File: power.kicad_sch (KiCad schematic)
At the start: 62 parts, among them Q2 NTR5105PT1G, Q5 NX138BKWX, Q9 BC846BS

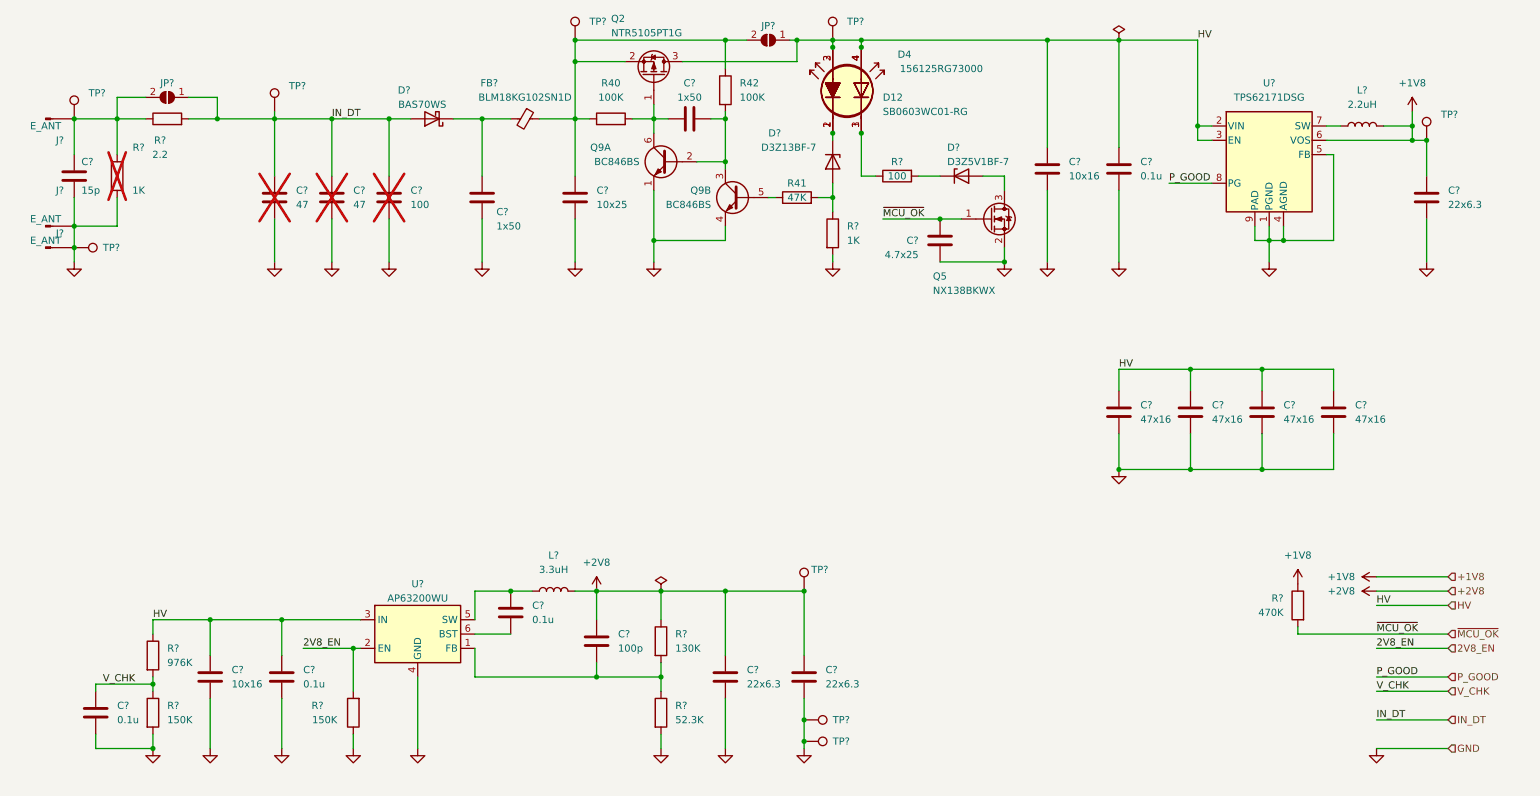
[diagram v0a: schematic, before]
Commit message: Fix capacitor values
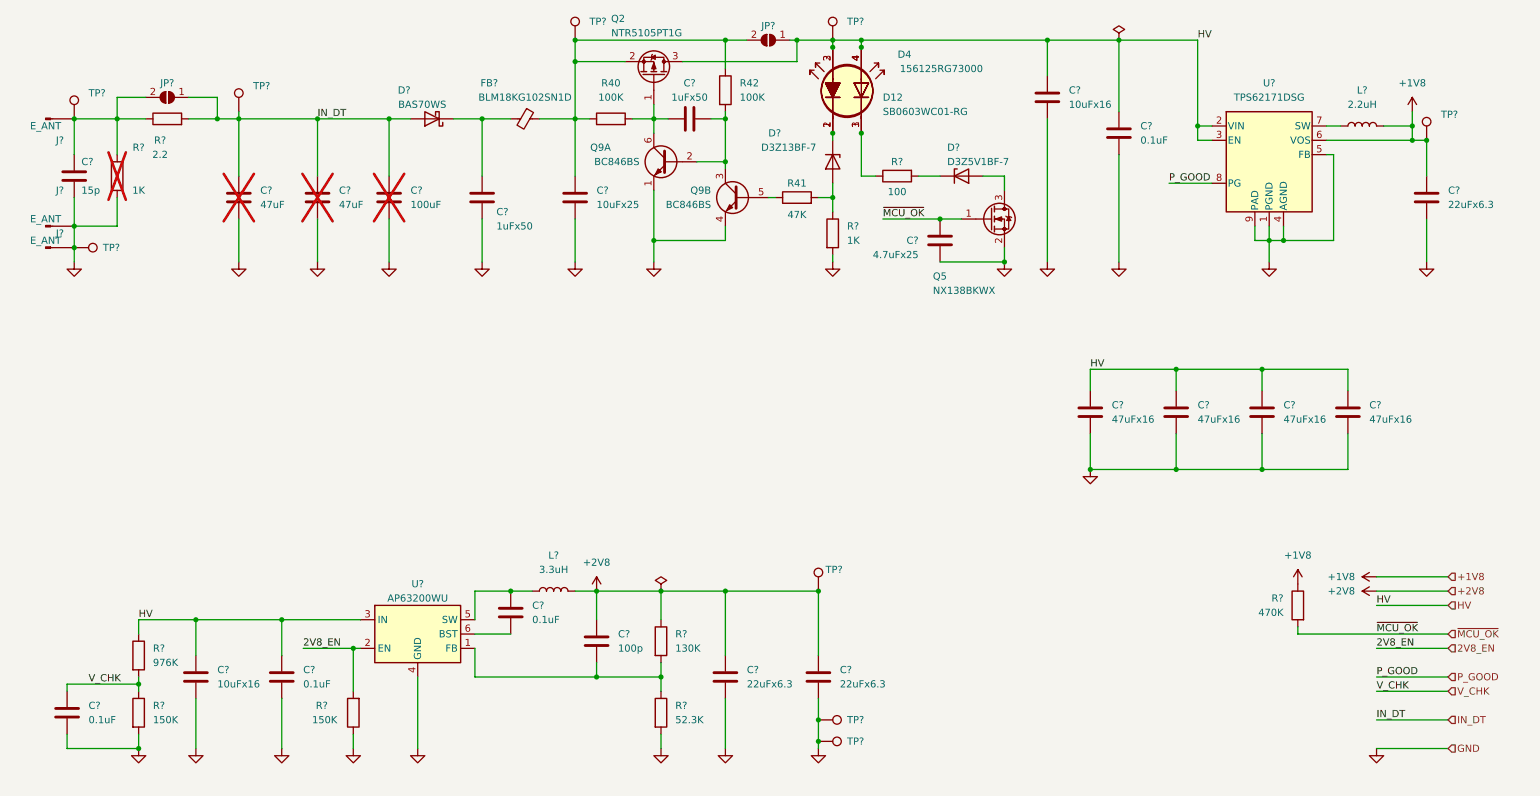
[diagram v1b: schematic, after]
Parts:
- C? (x2): value 1x50 -> 1uFx50
- C? (x4): value 47x16 -> 47uFx16
- C? (x4): value 0.1u -> 0.1uF
- C? (x3): value 22x6.3 -> 22uFx6.3
- C?: value 100 -> 100uF
- C? (x2): value 10x16 -> 10uFx16
- C?: value 10x25 -> 10uFx25
- C? (x2): value 47 -> 47uF
- C?: value 4.7x25 -> 4.7uFx25
- D?: value D3Z13BF-7 -> D3Z13BF-7
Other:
- moved on the sheet: C?, R?, TP?

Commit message: Fill up mouser part numbers
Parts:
- C? (x2): MouserPN (none) -> 81-GRM155R61H105ME5J
- C? (x4): MouserPN (none) -> 581-1210YG474ZAT2A
- C? (x4): MouserPN (none) -> 581-KGM05AR71C104KN
- C?: MouserPN (none) -> 187-CL05C101JC51PNC
- C? (x3): MouserPN (none) -> 581-KAM15CT70J226KT
- C?: MouserPN (none) -> 581-06035A150KAT2A
- C? (x3): now left out of the parts list
- C? (x2): MouserPN (none) -> 81-GRM188C81C106MA3D
- C?: MouserPN (none) -> 81-GRM188R61E106MA3D
- C?: MouserPN (none) -> 581-02013A100J
- D12: MouserPN (none) -> 593-SB0603WC01-RG
- D4: MouserPN (none) -> 710-156125RG73000
- D?: MouserPN (none) -> 241-BAS70WS_R1_00001
- D?: MouserPN (none) -> 621-D3Z5V1BF-7
- D?: MouserPN (none) -> 621-D3Z13BF-7
- FB?: MouserPN (none) -> 81-BLM18KG102SN1D
- L?: MouserPN (none) -> 710-74438335033
- Q2: MouserPN (none) -> 863-NTR5105PT1G
- Q5: MouserPN (none) -> 771-NX138BKWX
- Q9: MouserPN (none) -> 863-SBC846BDW1T1G
- U?: MouserPN (none) -> 595-TPS62171DSGR
- U?: MouserPN (none) -> 621-AP63200WU-7
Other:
- moved on the sheet: C?, D12, D4, D?, L?, Q5, Q9B, R41, R?, TP?, U?

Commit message: Finish BOM components filling
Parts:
- J? (x3), JP? (x2), TP? (x9): now left out of the parts list
- L?: MouserPN (none) -> 963-NR3015T2R2M
- R40, R42: MouserPN (none) -> 603-RC0402FR-7D100KL
- R41: MouserPN (none) -> 594-MCS04020C4702FE0
- R?: MouserPN (none) -> 71-CRCW0603-1.0K-E3
- R?: MouserPN (none) -> 603-RC0402FR-071KL
- R? (x2): MouserPN (none) -> 667-ERJ-2RKF1503X
- R?: MouserPN (none) -> 652-CR0402FX5232GLF
- R?: MouserPN (none) -> 71-CRCW06032R20FNEA
- R?: MouserPN (none) -> 603-RC0402FR-7D470KL
- R?: MouserPN (none) -> 603-RC0603FR-07976KL
- R?: MouserPN (none) -> 594-MCS04020C1000FE0
- R?: MouserPN (none) -> 652-CR0402FX-1303GLF
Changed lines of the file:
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@@
 			)
 		)
-		(property "MouserPN" ""
+		(property "MouserPN" "603-RC0402FR-7D100KL"
 			(at 123.19 38.1 0)
 			(effects
@@
 		(unit 1)
 		(exclude_from_sim no)
-		(in_bom yes)
+		(in_bom no)
 		(on_board yes)
 		(dnp no)
@@
 			)
 		)
-		(property "MouserPN" ""
+		(property "MouserPN" "71-CRCW0603-1.0K-E3"
 			(at 35.56 48.26 0)
 			(effects
@@
 		(unit 1)
 		(exclude_from_sim no)
-		(in_bom yes)
+		(in_bom no)
 		(on_board yes)
 		(dnp no)
@@
 		(unit 1)
 		(exclude_from_sim no)
-		(in_bom yes)
+		(in_bom no)
 		(on_board yes)
 		(dnp no)
@@
 		(unit 1)
 		(exclude_from_sim no)
-		(in_bom yes)
+		(in_bom no)
 		(on_board yes)
 		(dnp no)
@@
 			)
 		)
-		(property "MouserPN" ""
+		(property "MouserPN" "603-RC0402FR-071KL"
 			(at 162.56 66.04 0)
 			(effects
@@
 			)
 		)
-		(property "MouserPN" ""
+		(property "MouserPN" "667-ERJ-2RKF1503X"
 			(at 69.85 116.84 0)
 			(effects
@@
 		(unit 1)
 		(exclude_from_sim no)
-		(in_bom yes)
+		(in_bom no)
 		(on_board yes)
 		(dnp no)
@@
 		(unit 1)
 		(exclude_from_sim no)
-		(in_bom yes)
+		(in_bom no)
 		(on_board yes)
 		(dnp no)
@@
 			)
 		)
-		(property "MouserPN" ""
+		(property "MouserPN" "652-CR0402FX5232GLF"
 			(at 124.46 116.84 0)
 			(effects
@@
 			)
 		)
-		(property "MouserPN" ""
+		(property "MouserPN" "71-CRCW06032R20FNEA"
 			(at 44.45 38.1 0)
 			(effects
@@
 		(unit 1)
 		(exclude_from_sim no)
-		(in_bom yes)
+		(in_bom no)
 		(on_board yes)
 		(dnp no)
@@
 			)
 		)
-		(property "MouserPN" ""
+		(property "MouserPN" "603-RC0402FR-7D100KL"
 			(at 143.51 33.02 0)
 			(effects
@@
 		(unit 1)
 		(exclude_from_sim no)
-		(in_bom yes)
+		(in_bom no)
 		(on_board yes)
 		(dnp no)
@@
 		(unit 1)
 		(exclude_from_sim no)
-		(in_bom yes)
+		(in_bom no)
 		(on_board yes)
 		(dnp no)
@@
 		(unit 1)
 		(exclude_from_sim no)
-		(in_bom yes)
+		(in_bom no)
 		(on_board yes)
 		(dnp no)
@@
 			)
 		)
-		(property "MouserPN" ""
+		(property "MouserPN" "594-MCS04020C4702FE0"
 			(at 156.21 59.69 0)
 			(effects
@@
 			)
 		)
-		(property "MouserPN" ""
+		(property "MouserPN" "603-RC0402FR-7D470KL"
 			(at 232.41 128.27 0)
 			(effects
@@
 		(unit 1)
 		(exclude_from_sim no)
-		(in_bom yes)
+		(in_bom no)
 		(on_board yes)
 		(dnp no)
@@
 			)
 		)
-		(property "MouserPN" ""
+		(property "MouserPN" "667-ERJ-2RKF1503X"
 			(at 31.75 116.84 0)
 			(effects
@@
 			)
 		)
-		(property "MouserPN" ""
+		(property "MouserPN" "603-RC0603FR-07976KL"
 			(at 31.75 106.68 0)
 			(effects
@@
 		(unit 1)
 		(exclude_from_sim no)
-		(in_bom yes)
+		(in_bom no)
 		(on_board yes)
 		(dnp no)
@@
 			)
 		)
-		(property "MouserPN" ""
+		(property "MouserPN" "594-MCS04020C1000FE0"
 			(at 173.99 54.61 0)
 			(effects
@@
 			)
 		)
-		(property "MouserPN" ""
+		(property "MouserPN" "652-CR0402FX-1303GLF"
 			(at 124.46 104.14 0)
 			(effects
@@
 		(unit 1)
 		(exclude_from_sim no)
-		(in_bom yes)
+		(in_bom no)
 		(on_board yes)
 		(dnp no)
@@
 		(unit 1)
 		(exclude_from_sim no)
-		(in_bom yes)
+		(in_bom no)
 		(on_board yes)
 		(dnp no)
@@
 			)
 		)
-		(property "MouserPN" ""
+		(property "MouserPN" "963-NR3015T2R2M"
 			(at 256.54 39.37 0)
 			(effects
